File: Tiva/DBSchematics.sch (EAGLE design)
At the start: 24 parts, among them U1 TPS736XXDRB, Y1 16MHz, Y2 32.768kHz

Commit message: Excel Sheet updated
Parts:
- removed C1, C11, C12, C2, C6: 0.1uF, SparkFun-Capacitors:0.1UF-0402-16V-10%
- removed C13, C14: 10pF, SparkFun-Capacitors:10PF-0603-50V-5%
- removed C15, C16: 27pF, SparkFun-Capacitors:27PF-0603-50V-5%
- removed C18: 1.0uF, SparkFun-Capacitors:1.0UF-0402-16V-10%
- removed C7, C8, C9: 10nF, SparkFun-Capacitors:10NF-0603-50V-10%
- removed R1: 0, SparkFun-Resistors:0OHM-0603-1/10W-5%
- removed R2: 10k, SparkFun-Resistors:10KOHM-0603-1/10W-1%
- removed S1: PTS540, switch-ck:PTS540
- removed U1: TPS736XXDRB, texas:TPS736XXDRB
- added C4: 10uF, SparkFun-Capacitors:10UF-1206-6.3V-20%
- added IC1: LM1117IMPX-3.3, lm1117:LM1117IMPX-3.3
- C10: device SparkFun-Capacitors:1.0UF-0402-16V-10% -> SparkFun-Capacitors:1.0UF-1206-50V-10%
- C3: device SparkFun-Capacitors:2.2UF-0603-10V-20% -> SparkFun-Capacitors:2.2UF-1206-50V-10%
- C5: value 10nF -> 10uF; device SparkFun-Capacitors:10NF-0603-50V-10% -> SparkFun-Capacitors:10UF-1206-6.3V-20%
- Y1: device SparkFun-Clocks:CRYSTAL-16MHZSMD-5X3.2 -> SparkFun-Clocks:CRYSTAL-16MHZPTH-HC49US
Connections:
- removed net N$64: C15.1, C16.2
- removed net N$67: C5.1, U1.NR
- net GND: now also C4.2, C5.2, IC1.GND; no longer C1.2, C11.2, C12.2, C13.2, C14.1, C18.2, C2.2, C6.2, C7.2, C8.2, C9.2, S1.P, U1.GND
- net N$25: now also C4.1, IC1.IN; no longer C18.1, U1.EN, U1.IN
- net N$26: no longer C13.1, R1.2
- net N$27: no longer C15.2
- net N$28: no longer C16.1
- net N$3: no longer C14.2
- net RST: no longer R2.1
- net VCC: now also C5.1, IC1.OUT; no longer U1.OUT
- net VDD: no longer C1.1, C2.1, C6.1, C7.1, C8.1, C9.1, R1.1, R2.2, S1.S
- net VDDC: no longer C11.1, C12.1
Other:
- moved on the sheet: C5

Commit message: Work Continues
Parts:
- added C1, C11, C12, C13, C14, C2, C8: 0.01uF, SparkFun-Retired:2.2UF-CERCAP-10009
- added C15, C6: 24pF, SparkFun-Retired:2.2UF-CERCAP-10009
- added C16: 10pf, SparkFun-Retired:2.2UF-CERCAP-10009
- added C17: 10pF, SparkFun-Retired:2.2UF-CERCAP-10009
- added C18, C19: 0.1uF, SparkFun-Retired:2.2UF-CERCAP-10009
- added C20: 0.1uF, SparkFun-Capacitors:10UF-1206-6.3V-20%
- added C7: 2.2uF, SparkFun-Retired:2.2UF-CERCAP-10009
- added C9: 2.2uF, SparkFun-Capacitors:2.2UF-1206-50V-10%
- added D1: WHITE, SparkFun-LED:LED-WHITE1206
- added D2: GREEN, SparkFun-LED:LED-WHITE1206
- added D3: RED, SparkFun-LED:LED-WHITE1206
- added R1, R2: (no value), adafruit:R-US_M1206
- added R10: 10K, adafruit:R-US_M1206
- added R11: 3.3K, adafruit:R-US_M1206
- added R3, R4: 330, adafruit:R-US_M1206
- added R5, R8, R9: 4.7K, adafruit:R-US_M1206
- added R6, R7: 1K, adafruit:R-US_M1206
- added S1: Push Button, SparkFun-Retired:SWITCH-MOMENTARY-2-CLOSED
- added U$3: ADC128D818, ADC128D818:ADC128D818
- added U1: FT232RL, SparkFun-IC-Comms:FT232RL-BASICSSOP
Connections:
- removed net N$10: U$1.15, U$1.15'
- removed net N$11: U$1.16, U$1.16'
- removed net N$6: U$1.11, U$1.11'
- removed net N$7: U$1.12, U$1.12'
- removed net N$8: U$1.13, U$1.13'
- removed net N$9: U$1.14, U$1.14'
- new net N$64: C16.2, C17.1
- new net N$65: U$1.6, U1.VCC
- new net N$67: R4.1, U1.RXLED
- new net N$68: R3.2, U1.TXLED
- new net N$69: D3.A, R4.2
- new net N$70: D2.A, R3.1
- new net N$71: R5.2, U$3.INT
- new net N$72: R6.1, U$3.A0
- new net N$73: R7.1, U$3.A1
- new net N$74: R8.1, U$3.SDA
- new net N$75: R9.1, U$3.SCL
- new net N$76: U$3.VREF
- new net N$77: C20.1, U1.3V3OUT, U1.VCCIO
- new net PE0: U$1.11, U$1.11', U$2.9-PE0/AIN3/U7RX
- new net PE1: U$1.12, U$1.12', U$2.8-PE1/AIN2/U7TX
- new net PE2: U$1.15, U$1.15', U$2.7-PE2/AIN1
- new net PE3: U$1.16, U$1.16', U$2.6-PE3/AIN0
- new net RXD: U$2.16-PC4/C1-/IDX1/M0PWM6/U1RTS/U1RX/U4RX/WT0CCP0
- new net TXD: U$2.15-PC5/C1+M0PWM7/PHA1/U1CTS/U1TX/U4TX/WT0CCP1, U1.RXD
- new net VBAT: C18.1, C19.1, R10.1, R11.1, U$3.IN1
- new net ZIGBEERX: U$1.13, U$1.13', U$2.13-PC7/CO-/U3TX/USB0PFLT/WT1CCP1
- new net ZIGBEETX: U$1.14, U$1.14', U$2.14-PC6/C0+/PHB1/U3RX/USB0EPEN/WT1CCP0
- net GND: now also C1.2, C11.2, C12.2, C13.2, C14.2, C15.2, C19.2, C2.2, C20.2, C6.1, C7.2, C8.2, C9.2, D1.C, D2.C, D3.C, R11.2, R6.2, R7.2, S1.2, U$3.GND, U1.AGND, U1.GND1, U1.GND2, U1.GND3, U1.TEST
- net N$14: now also U$3.IN4
- net N$15: now also U$3.IN3
- net N$26: now also D1.A, R2.2; no longer Y1.1
- net N$27: now also C17.2
- net N$28: now also C16.1
- net N$3: now also C6.2
- net N$39: now also C18.2, R10.2
- net N$4: now also U1.USBDP
- net N$45: now also U$3.IN5
- net N$46: now also U$3.IN6
- net N$5: now also U1.USBDM
- net N$53: now also U$3.IN2
- net RST: now also C9.1, R1.2, S1.1
- net VCC: now also R2.1
- net VDD: now also C11.1, C12.1, C13.1, C14.1, C15.1, C7.1, C8.1, R5.1, R8.2, R9.2, U$3.V+, Y1.1
- net VDDC: now also C1.1, C2.1
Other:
- moved on the sheet: C10, C3, C4, C5, IC1

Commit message: Schematic Almost Complete
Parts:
- removed C18, C19: 0.1uF, SparkFun-Retired:2.2UF-CERCAP-10009
- added J1: 1X5, adafruit:1X5
- added Q1, Q2: BSS138, SparkFun:MOSFET-NCHANNELSMD
- added R12, R13, R14, R15, R16, R17, R18, R19: (no value), adafruit:R-US_M1206
- added R20, R21, R22, R23: 10K, SparkFun:RESISTOR1206
- added U2: LMV358, SparkFun-IC-Amplifiers:LMV358SOIC
- added U3: LMV324, SparkFun-IC-Amplifiers:LMV324
- R10: value 10K -> (none)
- R11: value 3.3K -> (none)
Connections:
- net N$58 renamed PF3
- net N$61 renamed PF4
- removed net N$22: U$1.63, U$1.63'
- removed net N$23: U$1.62, U$1.62'
- removed net N$32: U$1.23, U$1.23'
- removed net N$33: U$1.24, U$1.24'
- removed net N$34: U$1.25, U$1.25'
- removed net N$35: U$1.26, U$1.26'
- removed net N$36: U$1.27, U$1.27'
- removed net N$37: U$1.28, U$1.28'
- removed net N$38: U$1.29, U$1.29'
- removed net N$39: C18.2, R10.2, U$1.30, U$1.30'
- removed net N$40: U$1.31, U$1.31'
- removed net N$41: U$1.32, U$1.32'
- removed net N$45: U$1.37, U$1.37', U$3.IN5
- removed net N$46: U$1.38, U$1.38', U$3.IN6
- removed net N$47: U$1.39, U$1.39'
- removed net N$49: U$1.41, U$1.41'
- removed net N$50: U$1.42, U$1.42'
- removed net N$51: U$1.43, U$1.43'
- removed net N$52: U$1.44, U$1.44'
- removed net N$54: U$1.46, U$1.46'
- removed net N$59: U$1.55, U$1.55'
- removed net N$60: U$1.54, U$1.54'
- removed net N$62: U$1.52, U$1.52'
- removed net N$63: U$1.51, U$1.51'
- removed net N$74: R8.1, U$3.SDA
- removed net N$75: R9.1, U$3.SCL
- removed net VBAT: C18.1, C19.1, R10.1, R11.1, U$3.IN1
- removed net VCC: C5.1, IC1.OUT, R2.1
- new net 5V: U2G3.P$V+, U3G5.P$V+
- new net BUZZER: U$1.71, U$1.71', U$2.19-PA2/SSI0CLK
- new net DB4: U$1.26, U$1.26', U$2.43-PD4/U6RX/USB0DM/WT4CCP0
- new net DB5: U$1.25, U$1.25', U$2.44-PD5/U6TX/USB0DP/WT4CCP1
- new net DB6: U$1.27, U$1.27', U$2.53-PD6/M0FAULT0/PHA0/U2RX/WT5CCP0
- new net DB7: U$1.28, U$1.28', U$2.10-PD7/NMI/PHB0/U2TX/WT5CCP1
- new net EN: U$1.24, U$1.24', U$2.30-PF2/M0FAULT0/M1PWM6/SSI1CLK/TRDO
- new net HGHJ: R11.2, U2G1.-IN, U2G1.OUT
- new net LPE: Q1.D, R21.2, U$1.62, U$1.62'
- new net N$10: U$1.39, U$1.39', U$3.IN4
- new net N$11: J1.5, U$2.52-PC0/SWCLK/T4CCP0/TCK
- new net N$6: U2G2.-IN, U2G2.OUT
- new net N$7: U$1.70, U$1.70', U$3.IN7
- new net N$8: U$1.37, U$1.37', U$3.IN2
- new net N$9: U$1.38, U$1.38', U$3.IN3
- new net NO: C15.1, U$2.41-OSC1, Y1.1
- new net PA3: Q1.S, R20.2
- new net PA4: Q2.S, R22.2
- new net PA5: U$1.55, U$1.55', U$2.22-PA5/SSI0TX
- new net PA6: U$1.54, U$1.54', U$2.23-PA6/I2C1SCL/M1PWM2
- new net PB0: U$1.51, U$1.51', U$2.45-PB0/T2CCP0/U1RX/USB0ID
- new net PB1: U$1.52, U$1.52', U$2.46-PB1/T2CCP1/U1TX/USB0VBUS
- new net PB4: R10.1, R11.1, U$2.58-PB4/AIN10/CAN0RX/M0PWM2/SSI2CLK/T1CCP0
- new net PB5: U$1.46, U$1.46', U$2.57-PB5/AIN11/CAN0TX/M0PWM3/SSI2FSS/T1CCP1
- new net PD3: R16.1, R16.2, R17.1, U$2.64-PD3/AIN4/IDX0/SSI1TX/SSI3TX/USB0PFLT/WT3CCP1, U3G3.-IN, U3G3.OUT
- new net PE4: U$1.43, U$1.43', U$2.59-PE4/AIN9/CAN0RX/I2C2SCL/MOPWM2/U5RX
- new net PE5: U$1.42, U$1.42', U$2.60-PE5/AIN8/CAN0TX/I2C2SDA/M0PWM5/M1PWM3/U5TX
- new net POWER5: R21.1, R23.1, U$1.7
- new net RPE: Q2.D, R23.2, U$1.63, U$1.63'
- new net RS: U$1.22, U$1.22', U$2.28-PF0/C0O/CAN0RX/M1PWM4/NMI/PHA0/SSI1RX/T0CCP0/U1RTS
- new net RW: U$1.23, U$1.23', U$2.29-PF1/CL0/M1PWM5/PHB0/SSI1TX/T0CCP1/TRD1/U1CTS
- new net SCL: R9.1, U$2.47-PB2/I2C0SCL/T3CCP0, U$3.SCL
- new net SDA: R8.1, U$2.48-PB3/I2C0SDA/T3CCP1, U$3.SDA
- new net SHARP1: U$1.11, U$1.11', U3G1.+IN
- new net SHARP2: U$1.15, U$1.15', U3G2.+IN
- new net SHARP3: U$1.41, U$1.41', U3G3.+IN
- new net SHARP4: U$1.44, U$1.44', U3G4.+IN
- new net SHARP5: U$1.45, U$1.45', U2G1.+IN
- new net VBATTERY: C4.1, IC1.IN, U$1.29, U$1.29'
- new net WL1: U$1.30, U$1.30', U$2.63-PD2/AIN5/M0FAULT0/SSI1RX/SSI3RX/USB0EPEN/WT3CCP0
- new net WL2: U$1.31, U$1.31', U$2.62-PD1/AIN6/I2C3SDA/M0PWM7/M1PWM1/SSI1FSS/SSI3FSS/WT2CCP1
- new net WL3: U$1.32, U$1.32', U$2.61-PD0/AIN7/I2C3SCL/M0PWM6/M1PWM0/SSI1CLK/SSI3CLK/WT2CCP0
- new net WL4: U$3.IN1
- net GND: now also R10.2, R13.2, R15.2, R17.2, R19.2, U2G3.P$V-, U3G5.P$V-; no longer C19.2, R11.2
- net N$14: now also R18.2, U3G4.-IN, U3G4.OUT; no longer U$1.71, U$1.71', U$3.IN4
- net N$15: now also J1.4, U$2.51-PC1/SWDIO/T4CCP1/TMS; no longer U$1.70, U$1.70', U$3.IN3
- net N$16: now also U$3.IN6
- net N$2: now also U$3.IN0
- net N$25: now also J1.3, U$2.50-PC2/T5CCP0/TDI; no longer C4.1, IC1.IN, U$1.7
- net N$31: now also J1.2, U$2.49-PC3/SWO/T5CCP1/TDO; no longer U$1.22, U$1.22'
- net N$53: now also R18.1, R19.1, U$3.IN5; no longer U$1.45, U$1.45', U$3.IN2
- net PE0: now also R12.1, R12.2, R13.1, U3G1.-IN, U3G1.OUT; no longer U$1.11, U$1.11'
- net PE2: now also R14.1, R14.2, R15.1, U3G2.-IN, U3G2.OUT; no longer U$1.15, U$1.15'
- net RST: now also J1.1
- net VDD: now also C5.1, IC1.OUT, Q1.G, Q2.G, R2.1, R20.1, R22.1; no longer C15.1, Y1.1
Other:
- moved on the sheet: R10, R11

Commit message: Progress Presentation I
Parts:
- removed J1: 1X5, adafruit:1X5
- added JP1: (no value), adafruit:PINHD-1X8-3.5MM
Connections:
- net N$64 renamed GNDX
- removed net N$76: U$3.VREF
- new net RX: JP1.2, U$2.17-PA0/CAN1RX/U0RX
- new net SERVO1: U$2.1-PB6/M0PWM0/SSI2RX/T0CCP0
- new net SERVO2: U$2.4-PB7/M0PWM1/SSI2TX/T0CCP1
- new net SERVO3: U$2.24-PA7/I2C1SDA/M1PWM3
- new net TX: JP1.3, U$2.18-PA1/CAN1TX/U0TX
- net GND: no longer U$2.32-WAKE
- net N$11: now also JP1.8; no longer J1.5
- net N$15: now also JP1.7; no longer J1.4
- net N$25: now also JP1.6; no longer J1.3
- net N$31: now also JP1.5; no longer J1.2
- net PA3: now also U$2.20-PA3/SSI0FSS
- net PA4: now also U$2.21-PA4/SSIORX
- net PF3: now also U$2.31-PF3/CAN0TX/M1PWM7/SSI1FSS/T1CCP1/TRCLK
- net RST: now also JP1.1; no longer J1.1
- net VDD: now also R1.1, U$3.VREF
- net VDDC: now also U$2.56-VDDC
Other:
- note added: "EXT DBG"
- note added: "RST"
- note added: "RXD"
- note added: "TCK"
- note added: "TDI"
- note added: "TDO"
- note added: "TMS"
- note added: "TXD"
- moved on the sheet: C1, C10, C16, C17, C2, C3, R6, Y2

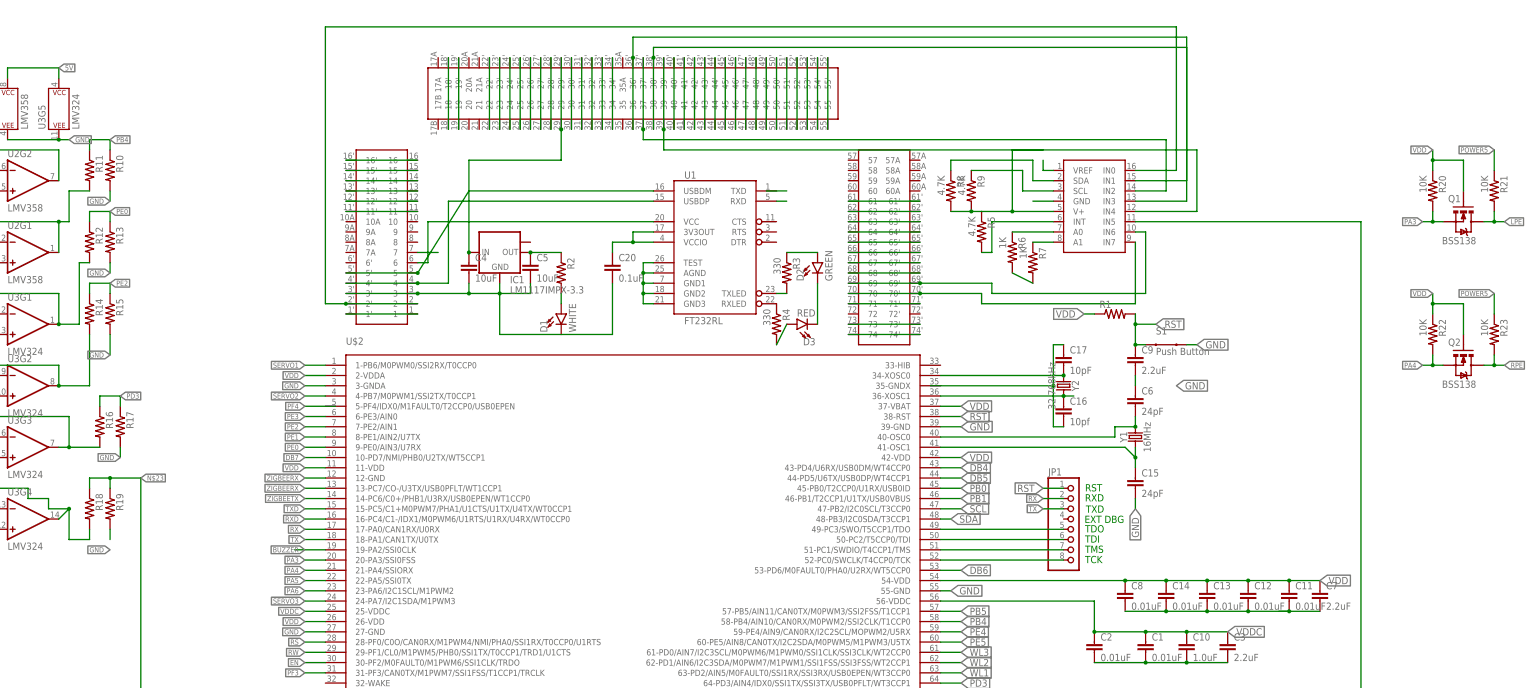
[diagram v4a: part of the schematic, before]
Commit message: Port Expander Added
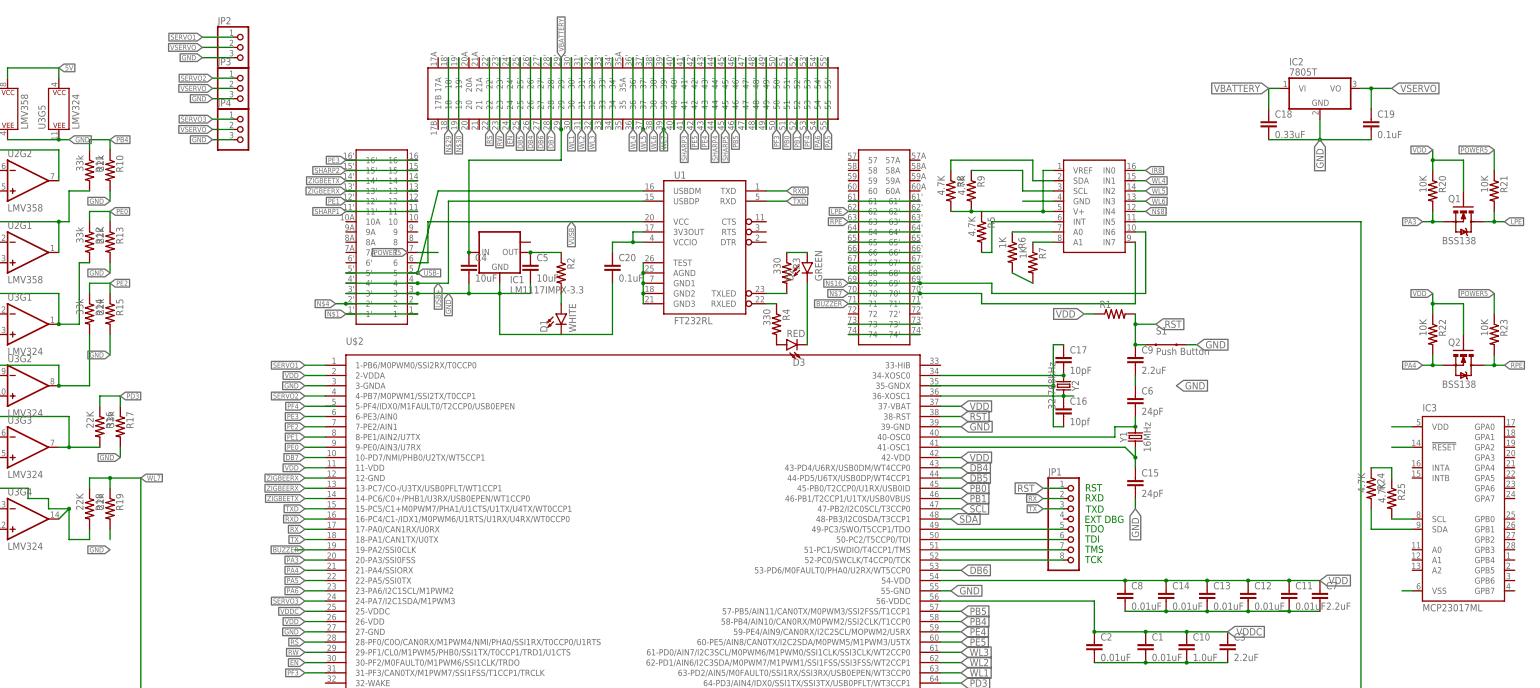
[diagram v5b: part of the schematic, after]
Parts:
- added C18: 0.33uF, SparkFun-Retired:2.2UF-CERCAP-10009
- added C19: 0.1uF, SparkFun-Retired:2.2UF-CERCAP-10009
- added IC2: 7805T, adafruit:7805T
- added IC3: MCP23017ML, adafruit:MCP23017ML
- added JP2, JP3, JP4: (no value), adafruit:PINHD-1X3
- added R24, R25: 4.7K, adafruit:R-US_M1206
- R10, R15, R19: value (none) -> 22k
- R11, R12, R14, R17: value (none) -> 33k
- R13, R16, R18: value (none) -> 22K
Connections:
- net N$4 renamed USB+
- net N$5 renamed USB-
- net N$65 renamed VUSB
- net N$8 renamed WL5
- net N$9 renamed WL6
- removed net N$10: U$1.39, U$1.39', U$3.IN4
- removed net N$2: U$1.2, U$1.2', U$3.IN0
- removed net N$23: R18.1, R19.1, U$3.IN5
- removed net N$44: U$1.36, U$1.36'
- new net IR8: U$3.IN0
- new net N$4: U$1.2, U$1.2'
- new net N$8: U$3.IN4
- new net VSERVO: C19.1, IC2.VO, JP2.2, JP3.2, JP4.2
- new net WL7: R18.1, R19.1, U$1.39, U$1.39', U$3.IN5
- net GND: now also C18.2, C19.2, IC2.GND, IC3.VSS, JP2.3, JP3.3, JP4.3
- net RST: now also IC3.!RESET
- net RXD: now also U1.TXD
- net SCL: now also IC3.SCL, R25.2
- net SDA: now also IC3.SDA, R24.2
- net SERVO1: now also JP2.1
- net SERVO2: now also JP3.1
- net SERVO3: now also JP4.1
- net VBATTERY: now also C18.1, IC2.VI
- net VDD: now also IC3.VDD, R24.1, R25.1
- net WL4: now also U$1.36, U$1.36'
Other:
- moved on the sheet: D2, D3, U1

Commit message: Layout
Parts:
- removed R24, R25: 4.7K, adafruit:R-US_M1206
- added JP5, JP6: (no value), adafruit:PINHD-1X8BIG
- added JP7, JP8: (no value), adafruit:PINHD-1X1
- C18: value 0.33uF -> 100uF; device SparkFun-Retired:2.2UF-CERCAP-10009 -> adafruit:C-US025-024X044
- IC1: value LM1117IMPX-3.3 -> LM1117-3.3
- IC3: value MCP23017ML -> MCP23017SO; device adafruit:MCP23017ML -> adafruit:MCP23017SO
- R1: value (none) -> 10K
- R10, R19: value 22k -> 33K
- R11, R12: value 33k -> 22K
- R13: value 22K -> 33K
- R14: value 33k -> 22k
- R15: value 22k -> 33k
- R2: value (none) -> 330
- R8: value 4.7K -> 10K
- R9: value 4.7K -> 10k
- S1: device SparkFun-Retired:SWITCH-MOMENTARY-2-CLOSED -> SparkFun-Switches:MOMENTARY-SWITCH-SPST-PTH-6.0MM
- renumbered JP2 to SERVO1, JP3 to SERVO2, JP4 to SERVO3
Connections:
- removed net 5V: U2G3.P$V+, U3G5.P$V+
- removed net N$4: U$1.2, U$1.2'
- removed net POWER5: R21.1, R23.1, U$1.7
- removed net RW: U$1.23, U$1.23', U$2.29-PF1/CL0/M1PWM5/PHB0/SSI1TX/T0CCP1/TRD1/U1CTS
- new net EXTSHARP: R18.1, R19.1, U$3.IN5
- new net FDSFSDF: R12.2, U3G1.-IN, U3G1.OUT
- new net INTAB: IC3.INTA, IC3.INTB, U$2.29-PF1/CL0/M1PWM5/PHB0/SSI1TX/T0CCP1/TRD1/U1CTS
- new net N$10: IC3.GPA4, JP5.5
- new net N$2: IC3.GPA0, JP5.1
- new net N$23: IC3.GPA5, JP5.6
- new net N$32: IC3.GPA6, JP5.7
- new net N$33: IC3.GPA7, JP5.8
- new net N$34: IC3.GPB0, JP6.1
- new net N$35: IC3.GPB1, JP6.2
- new net N$36: IC3.GPB2, JP6.3
- new net N$37: IC3.GPB3, JP6.4
- new net N$38: IC3.GPB4, JP6.5
- new net N$39: IC3.GPB5, JP6.6
- new net N$40: IC3.GPB6, JP6.7
- new net N$41: IC3.GPB7, JP6.8
- new net N$5: IC3.GPA1, JP5.2
- new net N$9: IC3.GPA3, JP5.4
- new net SDFSDFSD: R14.2, U3G2.-IN, U3G2.OUT
- new net XXVX: R16.2, U3G3.-IN, U3G3.OUT
- net GND: now also IC3.A0, IC3.A1, IC3.A2, U$1.23, U$1.23'
- net GNDX: now also U$2.35-GNDX
- net IR8: now also U$1.2, U$1.2'
- net N$8: now also IC3.GPA2, JP5.3; no longer U$3.IN4
- net PD3: no longer R16.2, U3G3.-IN, U3G3.OUT
- net PE0: no longer R12.2, U3G1.-IN, U3G1.OUT
- net PE2: no longer R14.2, U3G2.-IN, U3G2.OUT
- net PF4: now also U$2.5-PF4/IDX0/M1FAULT0/T2CCP0/USB0EPEN
- net SCL: now also JP7.1; no longer R25.2
- net SDA: now also JP8.1; no longer R24.2
- net VDD: no longer R24.1, R25.1
- net VSERVO: now also R21.1, R23.1, U2G3.P$V+, U3G5.P$V+
- net WL7: now also U$3.IN4; no longer R18.1, R19.1, U$3.IN5
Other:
- moved on the sheet: C20

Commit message: Layout Complete
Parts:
- added 3.3V, 5V, GND: (no value), adafruit:PINHD-1X1
- added JP9: GND, adafruit:PINHD-1X1
- U$2: value TM4C123GH6PMS-PQFP-G64 -> TM4C123GH6PM
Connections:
- net GND: now also GND.1, JP1.4, JP9.1
- net VDD: now also 3.3V.1
- net VSERVO: now also 5V.1
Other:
- note added: "GND"
- note removed: "EXT DBG"
